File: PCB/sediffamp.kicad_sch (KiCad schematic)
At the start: 17 parts, among them U12 OPA1622, U13 OPA1622, U14 OPA1622

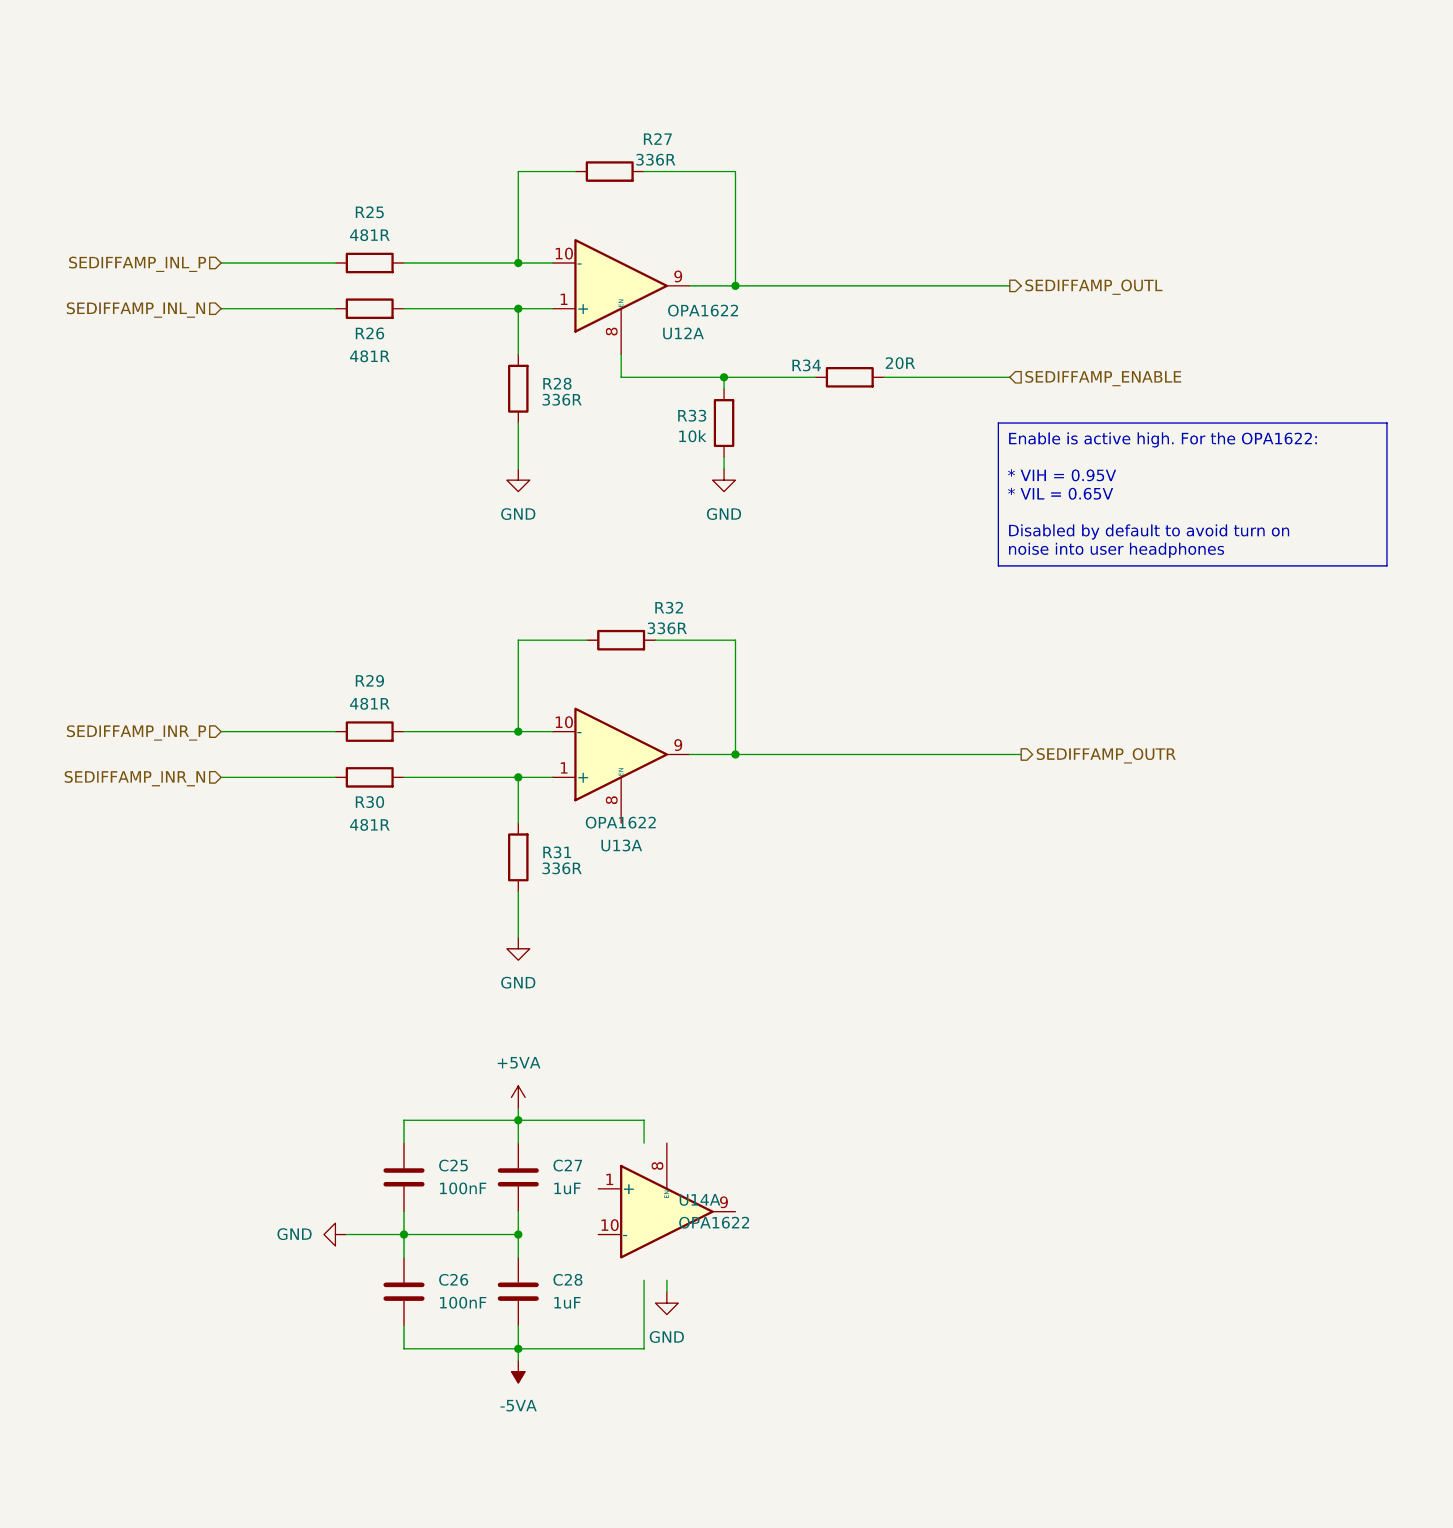
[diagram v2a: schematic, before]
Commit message: Finished basic placement
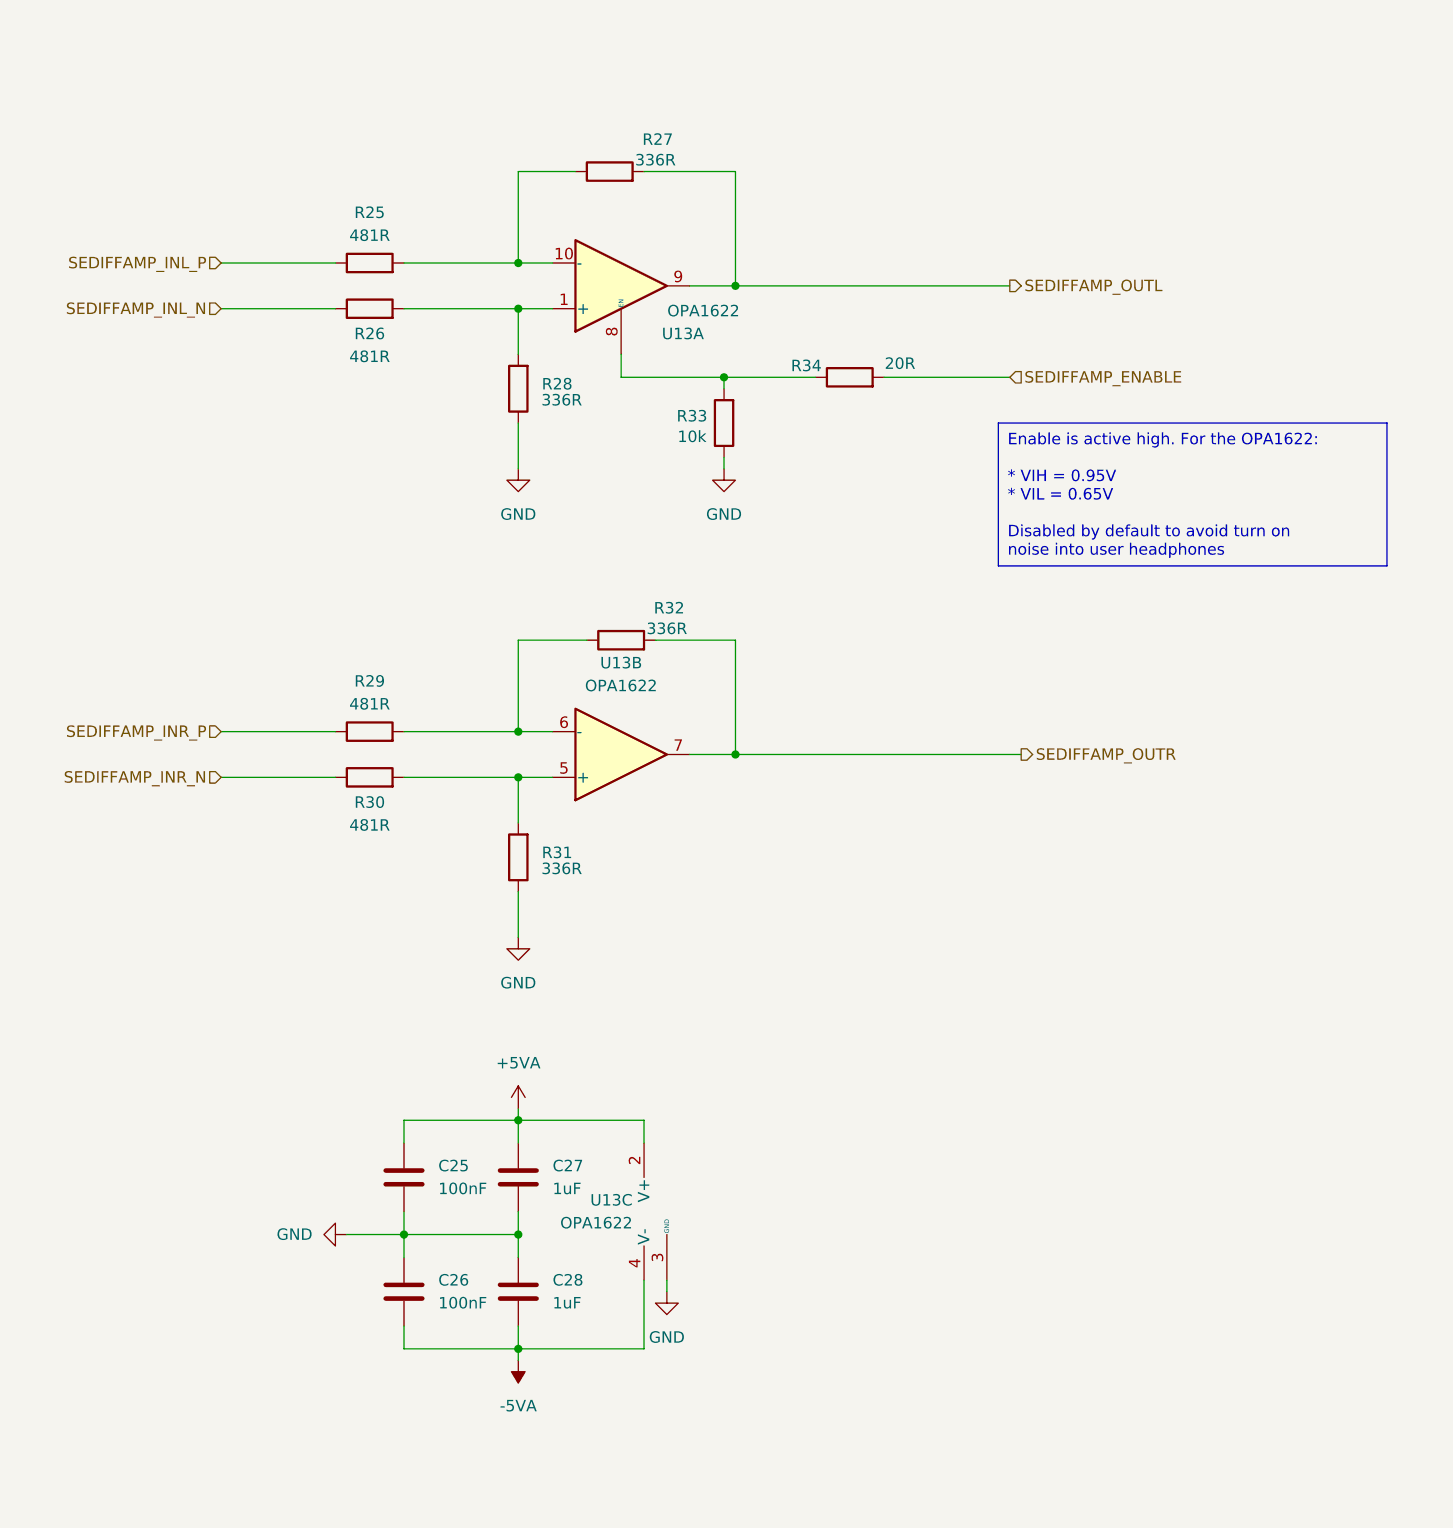
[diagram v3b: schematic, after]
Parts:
- removed U14: OPA1622, Package_SON:Texas_S-PVSON-N10, symbol Amplifier_Audio:OPA1622
- added unit 3 of U13
- renumbered U12 to U13
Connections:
- net +5VA: now also U13.2 (V+)
- net -5VA: now also U13.11 (V-), U13.4 (V-)
- net GND: now also U13.3 (GND)
- net SEDIFFAMP_OUTR: now also U13.7; no longer U13.9
- net at R30.2, R31.2: now also U13.5 (+); no longer U13.1 (+)
- net at R29.2, R32.1: now also U13.6 (-); no longer U13.10 (-)
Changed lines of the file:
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@@
+	(symbol
+		(lib_id "Amplifier_Audio:OPA1622")
+		(at 144.78 156.21 0)
+		(unit 3)
+		(exclude_from_sim no)
+		(in_bom yes)
+		(on_board yes)
+		(dnp no)
+		(fields_autoplaced yes)
+		(property "Reference" "U13"
+			(at 140.97 154.9399 0)
+			(effects
+				(font
+					(size 1.27 1.27)
+				)
+				(justify right)
+			)
+		)
+		(property "Value" "OPA1622"
+			(at 140.97 157.4799 0)
+			(effects
+				(font
+					(size 1.27 1.27)
+				)
+				(justify right)
+			)
+		)
+		(property "Footprint" "Package_SON:Texas_S-PVSON-N10"
+			(at 144.78 166.37 0)
+			(effects
+				(font
+					(size 1.27 1.27)
+				)
+				(hide yes)
+			)
+		)
+		(property "Datasheet" "http://www.ti.com/lit/ds/symlink/opa1622.pdf"
+			(at 144.78 156.21 0)
+			(effects
+				(font
+					(size 1.27 1.27)
+				)
+				(hide yes)
+			)
+		)
+		(property "Description" "High-Fidelity, Bipolar-Input, Audio Operational Amplifier, VSON-10"
+			(at 144.78 156.21 0)
+			(effects
+				(font
+					(size 1.27 1.27)
+				)
+				(hide yes)
+			)
+		)
+		(pin "4"
+		)
+		(pin "1"
+		)
+		(pin "2"
+		)
+		(pin "10"
+		)
+		(pin "3"
+		)
+		(pin "8"
+		)
+		(pin "6"
+		)
+		(pin "9"
+		)
+		(pin "11"
+		)
+		(pin "7"
+		)
+		(pin "5"
+		)
+		(instances
+			(project "mhd314"
+				(path "/afee45fc-2361-4efb-9cde-757fc2efd57b/913309c3-489c-42b3-afc6-179d92cffcea/e26c83d8-adef-4edb-bc93-065fe5f245aa"
+					(reference "U13")
+					(unit 3)
+				)
+			)
+		)
+	)
 	(symbol
 		(lib_id "Amplifier_Audio:OPA1622")
 		(at 139.7 105.41 0)
 		(mirror x)
-		(unit 1)
+		(unit 2)
 		(exclude_from_sim no)
 		(in_bom yes)
@@
 		(fields_autoplaced yes)
 		(property "Reference" "U13"
-			(at 139.7 115.57 0)
+			(at 139.7 95.25 0)
 			(effects
 				(font
@@
 		)
 		(property "Value" "OPA1622"
-			(at 139.7 113.03 0)
+			(at 139.7 97.79 0)
 			(effects
 				(font
@@
 				(path "/afee45fc-2361-4efb-9cde-757fc2efd57b/913309c3-489c-42b3-afc6-179d92cffcea/e26c83d8-adef-4edb-bc93-065fe5f245aa"
 					(reference "U13")
-					(unit 1)
+					(unit 2)
 				)
 			)
@@
 		(on_board yes)
 		(dnp no)
-		(property "Reference" "U12"
+		(property "Reference" "U13"
 			(at 146.558 58.674 0)
 			(effects
@@
 			(project "mhd314"
 				(path "/afee45fc-2361-4efb-9cde-757fc2efd57b/913309c3-489c-42b3-afc6-179d92cffcea/e26c83d8-adef-4edb-bc93-065fe5f245aa"
-					(reference "U12")
+					(reference "U13")
 					(unit 1)
 				)
@@
 					(unit 1)
 				)
-			)
-		)
-	)
-	(symbol
-		(lib_id "Amplifier_Audio:OPA1622")
-		(at 144.78 156.21 0)
-		(unit 1)
-		(exclude_from_sim no)
-		(in_bom yes)
-		(on_board yes)
-		(dnp no)
-		(fields_autoplaced yes)
-		(property "Reference" "U14"
-			(at 146.05 154.9399 0)
-			(effects
-				(font
-					(size 1.27 1.27)
-				)
-				(justify left)
-			)
-		)
-		(property "Value" "OPA1622"
-			(at 146.05 157.4799 0)
-			(effects
-				(font
-					(size 1.27 1.27)
-				)
-				(justify left)
-			)
-		)
-		(property "Footprint" "Package_SON:Texas_S-PVSON-N10"
-			(at 144.78 166.37 0)
-			(effects
-				(font
-					(size 1.27 1.27)
-				)
-				(hide yes)
-			)
-		)
-		(property "Datasheet" "http://www.ti.com/lit/ds/symlink/opa1622.pdf"
-			(at 144.78 156.21 0)
-			(effects
-				(font
-					(size 1.27 1.27)
-				)
-				(hide yes)
-			)
-		)
-		(property "Description" "High-Fidelity, Bipolar-Input, Audio Operational Amplifier, VSON-10"
-			(at 144.78 156.21 0)
-			(effects
-				(font
-					(size 1.27 1.27)
-				)
-				(hide yes)
-			)
-		)
-		(pin "4"
-		)
-		(pin "1"
-		)
-		(pin "2"
-		)
-		(pin "10"
-		)
-		(pin "3"
-		)
-		(pin "8"
-		)
-		(pin "6"
-		)
-		(pin "9"
-		)
-		(pin "11"
-		)
-		(pin "7"
-		)
-		(pin "5"
-		)
-		(instances
-			(project "mhd314"
-				(path "/afee45fc-2361-4efb-9cde-757fc2efd57b/913309c3-489c-42b3-afc6-179d92cffcea/e26c83d8-adef-4edb-bc93-065fe5f245aa"
-					(reference "U14")
-					(unit 1)
-				)

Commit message: Routing revised, added some missing parameters to components
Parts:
- C27, C28: Voltage 6.3V -> 16V
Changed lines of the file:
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@@
 			)
 		)
-		(property "Voltage" "6.3V"
+		(property "Voltage" "16V"
 			(at 128.27 152.4 0)
 			(effects
@@
 			)
 		)
-		(property "Voltage" "6.3V"
+		(property "Voltage" "16V"
 			(at 128.27 165.1 0)
 			(effects

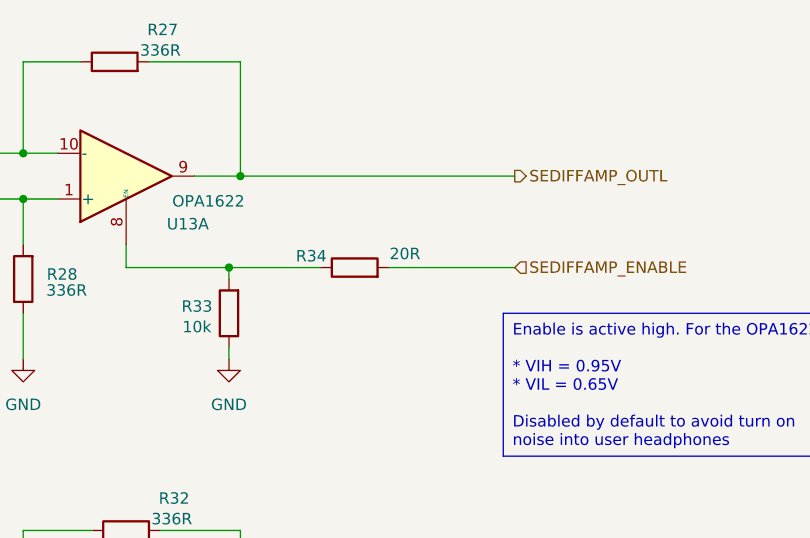
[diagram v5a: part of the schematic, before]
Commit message: Updated PCB with digital traxce suggestions. Added JLCPCB Pns
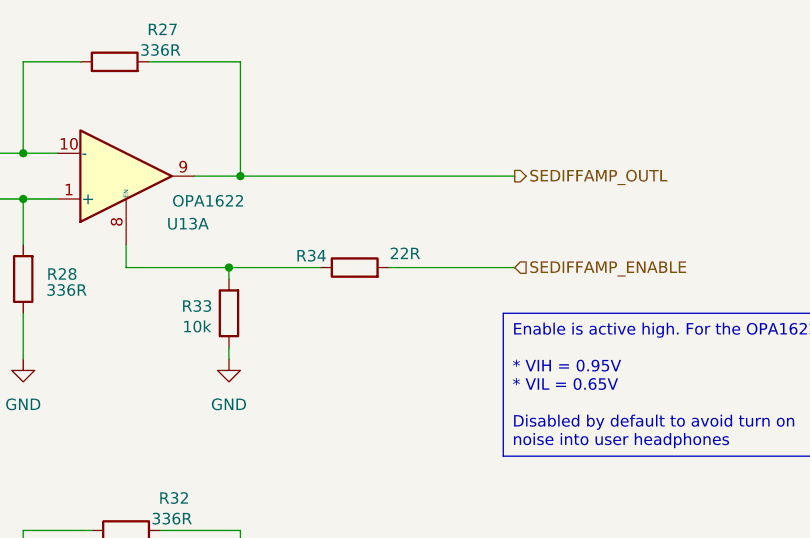
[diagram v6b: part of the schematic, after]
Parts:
- C25, C26: JLCPCBPn (none) -> C1525; Voltage 25V -> 16V
- C27, C28: JLCPCBPn (none) -> C15849
- R33: JLCPCBPn (none) -> C25744
- R34: value 20R -> 22R; JLCPCBPn (none) -> C25092
- U13: JLCPCBPn (none) -> C2876559
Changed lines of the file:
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@@
+			)
+		)
+		(property "JLCPCBPn" "C25744"
+			(at 151.13 68.58 0)
+			(effects
+				(font
+					(size 1.27 1.27)
+				)
+				(hide yes)
 			)
 		)
@@
 		)
 		(property "Description" "High-Fidelity, Bipolar-Input, Audio Operational Amplifier, VSON-10"
+			(at 144.78 156.21 0)
+			(effects
+				(font
+					(size 1.27 1.27)
+				)
+				(hide yes)
+			)
+		)
+		(property "JLCPCBPn" "C2876559"
 			(at 144.78 156.21 0)
 			(effects
@@
 			)
 		)
+		(property "JLCPCBPn" "C2876559"
+			(at 139.7 105.41 0)
+			(effects
+				(font
+					(size 1.27 1.27)
+				)
+				(hide yes)
+			)
+		)
 		(pin "4"
 		)
@@
 			)
 		)
+		(property "JLCPCBPn" "C2876559"
+			(at 139.7 53.34 0)
+			(effects
+				(font
+					(size 1.27 1.27)
+				)
+				(hide yes)
+			)
+		)
 		(pin "4"
 		)
@@
 			)
 		)
+		(property "JLCPCBPn" "C15849"
+			(at 128.27 152.4 0)
+			(effects
+				(font
+					(size 1.27 1.27)
+				)
+				(hide yes)
+			)
+		)
 		(pin "1"
 		)
@@
 			)
 		)
-		(property "Value" "20R"
+		(property "Value" "22R"
 			(at 170.688 61.976 90)
 			(effects
@@
 		(property "Tolerance" "5%"
 			(at 165.1 63.5 90)
+			(effects
+				(font
+					(size 1.27 1.27)
+				)
+				(hide yes)
+			)
+		)
+		(property "JLCPCBPn" "C25092"
+			(at 165.1 63.5 0)
 			(effects
 				(font
@@
 			)
 		)
-		(property "Voltage" "25V"
+		(property "Voltage" "16V"
+			(at 115.57 152.4 0)
+			(effects
+				(font
+					(size 1.27 1.27)
+				)
+				(hide yes)
+			)
+		)
+		(property "JLCPCBPn" "C1525"
 			(at 115.57 152.4 0)
 			(effects
@@
 			)
 		)
+		(property "JLCPCBPn" "C15849"
+			(at 128.27 165.1 0)
+			(effects
+				(font
+					(size 1.27 1.27)
+				)
+				(hide yes)
+			)
+		)
 		(pin "1"
 		)
@@
 			)
 		)
-		(property "Voltage" "25V"
+		(property "Voltage" "16V"
 			(at 115.57 165.1 0)
 			(effects
+				(font
+					(size 1.27 1.27)
+				)
+				(hide yes)
+			)
+		)
+		(property "JLCPCBPn" "C1525"
+			(at 115.57 165.1 0)
+			(effects
